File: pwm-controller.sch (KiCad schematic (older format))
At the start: 39 parts, among them J2 OUT-, J4 POWER, J5 OUT+, J6 DEBUG, J7 I2C, SW1 EC12D1524403, U1 78L05, U3 STM8S003F3Px

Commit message: ready to order?
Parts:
- removed J6: DEBUG, Connector_PinHeader_2.54mm:PinHeader_1x05_P2.54mm_Vertical, symbol Connector_Generic:Conn_01x05
- removed J7: I2C, Connector_PinHeader_2.54mm:PinHeader_2x05_P2.54mm_Vertical, symbol Connector_Generic:Conn_02x05_Odd_Even
- removed R10, R11, R13, R14, R19, R21, R22, R6, R7, R8, R9: 4.7k, Resistor_SMD:R_0402_1005Metric, symbol Device:R
- removed TP1: TP5V, TestPoint:TestPoint_Pad_D2.0mm, symbol Connector:TestPoint
- added C3: 3.3n, Capacitor_SMD:C_0402_1005Metric, symbol Device:C
- added D1: B5819W SL, Diode_SMD:D_SOD-123, symbol Device:D_Schottky
- added H3, H6: M2, MountingHole:MountingHole_2mm, symbol Mechanical:MountingHole
- added H8: M2, MountingHole:MountingHole_2.2mm_M2, symbol Mechanical:MountingHole
- added J1: DEBUG_ADDRESS_I2C_INT, Connector_PinHeader_2.54mm:PinHeader_2x09_P2.54mm_Horizontal, symbol Connector_Generic:Conn_02x09_Odd_Even
- added R1, R2: 220, Resistor_SMD:R_0402_1005Metric, symbol Device:R
- renumbered C6 to C1, C8 to C2, C1 to C4, C2 to C5, C7 to C6, C21 to C7, C22 to C8, C23 to C9, D1 to D2, D2 to D3, H5 to H4, H4 to H5, J2 to J6, R4 to R3, R5 to R4, R1 to R5, R3 to R6, R17 to R7, U3 to U1, U1 to U2
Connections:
- net GND: now also C3.1, J1.10 (Pin_10), J1.11 (Pin_11), J1.12 (Pin_12), J1.4 (Pin_4), J1.6 (Pin_6), J1.8 (Pin_8)
- net INT: now also C3.2, J1.13 (Pin_13), J1.14 (Pin_14)
- net PWM1: now also U1.10 (PA3/PWM1); no longer U1.20 (PD3/PWM2)
- net PWM2: now also U1.20 (PD3/PWM2); no longer U1.10 (PA3/PWM1)
- net RE_B: now also U1.13 (PC3/RE_B); no longer U1.19 (PD2/SADD0)
- net RE_I: now also U1.15 (PC5/RE_I); no longer U1.16 (PC6/SADD2)
- net RE_Q: now also U1.14 (PC4/RE_Q); no longer U1.17 (PC7/SADD1)
- net SADD0: now also U1.19 (PD2/SADD0), J1.5 (Pin_5); no longer U1.15 (PC5/RE_I)
- net SADD1: now also U1.17 (PC7/SADD1), J1.7 (Pin_7); no longer U1.14 (PC4/RE_Q)
- net SADD2: now also U1.16 (PC6/SADD2), J1.9 (Pin_9); no longer U1.13 (PC3/RE_B)
- net SCL: now also J1.15 (Pin_15), J1.16 (Pin_16), R1.1; no longer U1.12 (PB4/SCL)
- net SDA: now also J1.17 (Pin_17), J1.18 (Pin_18), R2.1; no longer U1.11 (PB5/SDA)
- net SWIM: now also J1.2 (Pin_2)
- net URX: now also J1.1 (Pin_1)
- net UTX: now also J1.3 (Pin_3)
- net VIN: now also D1.2 (A); no longer C4.1, U2.3 (IN)
- new net SCL_PIN: R1.2, U1.12 (PB4/SCL)
- new net SDA_PIN: R2.2, U1.11 (PB5/SDA)
- new net VIN_D: C4.1, D1.1 (K), U2.3 (IN)
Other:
- note added: "I2C"
- note added: "INT is I2C interrupt for\nslaves to callback on.\ne.g. on user input / boot."
- note added: "IO connector"
- note added: "MCU:\n - Table 21: 5mA @ 16MHz / 1mA @ 2MHz / <1mA @ 128kHz\n - Peripherals approx 1mA extra.\nGPIO: 1mA max loading, per 4.7kΩ pullup\n\nInternal pullups 30-80kΩ (§9.3.6)."
- note removed: "Debug"
- note removed: "I2C and master/slave/address config"
- note removed: "INT is I2C interrupt for\nslaves to callback on."
- note removed: "MCU:\n - Table 21: 5mA @ 16MHz / 1mA @ 2MHz / <1mA @ 128kHz\n - Peripherals approx 1mA extra.\nGPIO: 1mA max loading, per 4.7kΩ pullup\n\nInternal pullups 30-80kΩ (§9.3.6), could use those\nfor all except I2C, instead of 4.7kΩ resistors. Would\nconsiderably improve the routing."
- note removed: "Slave interrupt"
- moved on the sheet: C1, C2, C4, C5, C6, C7, C8, C9, H1, H2, H4, H5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

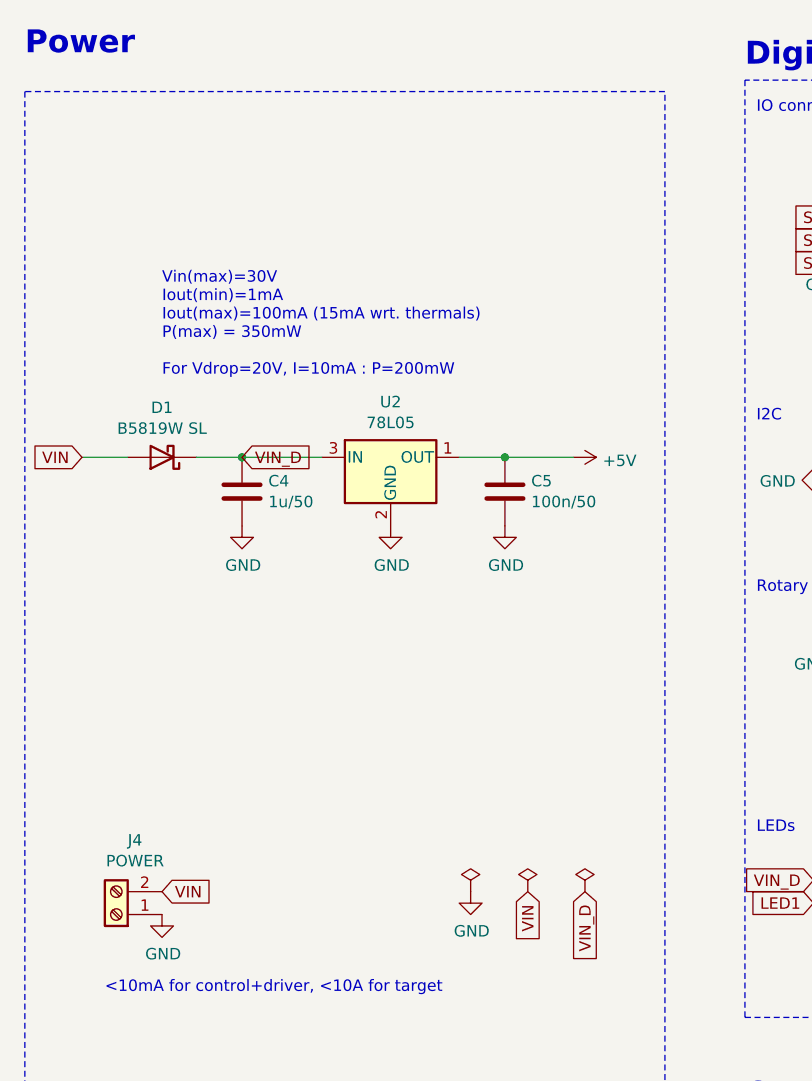
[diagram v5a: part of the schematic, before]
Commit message: moved screw terminals to edge of board, reduced stitching/thermal-via frequency
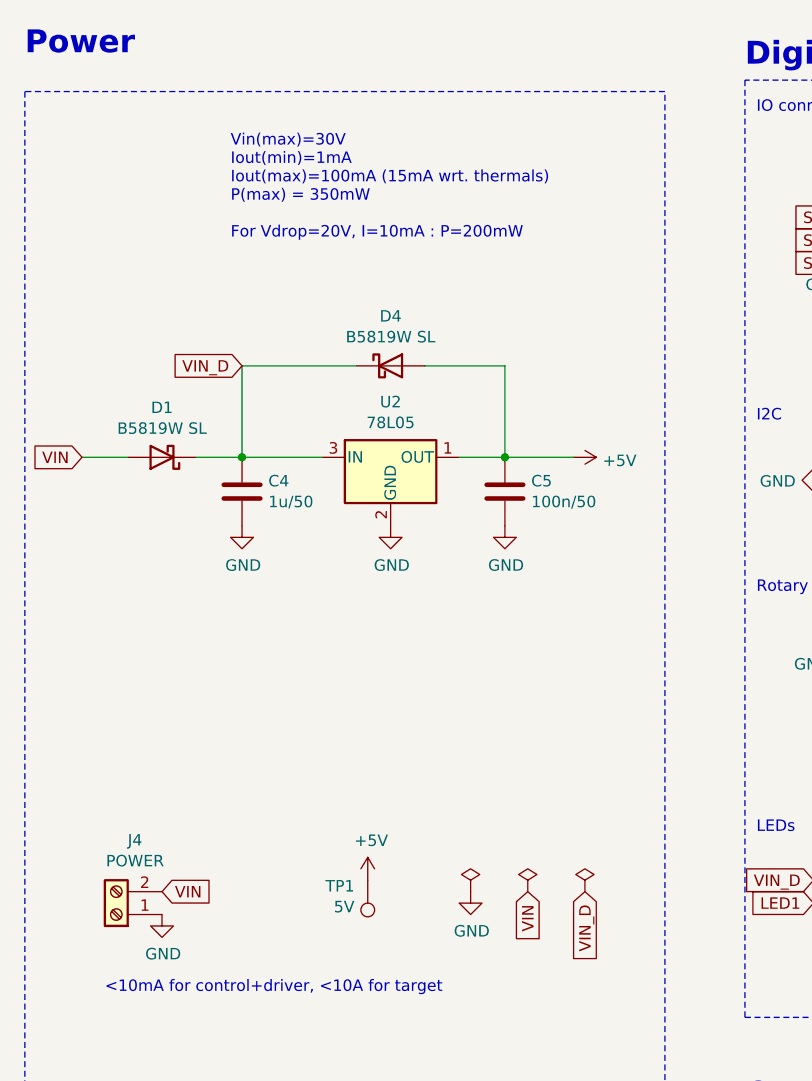
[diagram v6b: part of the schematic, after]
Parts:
- added D4: B5819W SL, Diode_SMD:D_SOD-123, symbol Device:D_Schottky
- added TP1: 5V, TestPoint:TestPoint_THTPad_D1.5mm_Drill0.7mm, symbol Connector:TestPoint
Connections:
- net +5V: now also D4.2 (A), TP1.1
- net VIN_D: now also D4.1 (K)
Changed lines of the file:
@@
 	1    0    0    -1
 $EndComp
-Wire Wire Line
-	2700 3450 2900 3450
 Connection ~ 2900 3450
 $Comp
@@
 Text GLabel 1050 3450 0    50   Input ~ 0
 VIN
-Text Notes 1400 3100 0    50   ~ 0
+Text Notes 1700 2500 0    50   ~ 0
 Vin(max)=30V\nIout(min)=1mA\nIout(max)=100mA (15mA wrt. thermals)\nP(max) = 350mW\n\nFor Vdrop=20V, I=10mA : P=200mW
 $Comp
@@
 Wire Wire Line
 	1250 3450 1050 3450
-Text GLabel 1750 3450 2    50   Input ~ 0
+Text GLabel 1750 3050 0    50   Input ~ 0
 VIN_D
 $Comp
@@
 Text GLabel 5950 3650 2    50   Input ~ 0
 SDA
+$Comp
+L Device:D_Schottky D4
+U 1 1 622155D1
+P 2400 3050
+F 0 "D4" H 2400 3267 50  0000 C CNN
+F 1 "B5819W SL" H 2400 3176 50  0000 C CNN
+F 2 "Diode_SMD:D_SOD-123" H 2400 3050 50  0001 C CNN
+F 3 "https://datasheet.lcsc.com/lcsc/1809140216_Changjiang-Electronics-Tech--CJ-B5819W-SL_C8598.pdf" H 2400 3050 50  0001 C CNN
+F 4 "C8598" H 2400 3050 50  0001 C CNN "JLC"
+	1    2400 3050
+	1    0    0    -1
+$EndComp
+Wire Wire Line
+	2250 3050 1750 3050
+Wire Wire Line
+	1750 3050 1750 3450
+Wire Wire Line
+	2700 3450 2900 3450
+Wire Wire Line
+	2550 3050 2900 3050
+Wire Wire Line
+	2900 3050 2900 3450
+$Comp
+L power:+5V #PWR010
+U 1 1 6222B7D6
+P 2300 5300
+F 0 "#PWR010" H 2300 5150 50  0001 C CNN
+F 1 "+5V" H 2315 5473 50  0000 C CNN
+F 2 "" H 2300 5300 50  0001 C CNN
+F 3 "" H 2300 5300 50  0001 C CNN
+	1    2300 5300
+	1    0    0    -1
+$EndComp
+$Comp
+L Connector:TestPoint TP1
+U 1 1 6222D05A
+P 2300 5300
+F 0 "TP1" H 2358 5326 50  0000 L CNN
+F 1 "5V" H 2358 5417 50  0000 L CNN
+F 2 "TestPoint:TestPoint_THTPad_D1.5mm_Drill0.7mm" H 2500 5300 50  0001 C CNN
+F 3 "~" H 2500 5300 50  0001 C CNN
+	1    2300 5300
+	-1   0    0    1
+$EndComp
 $EndSCHEMATC

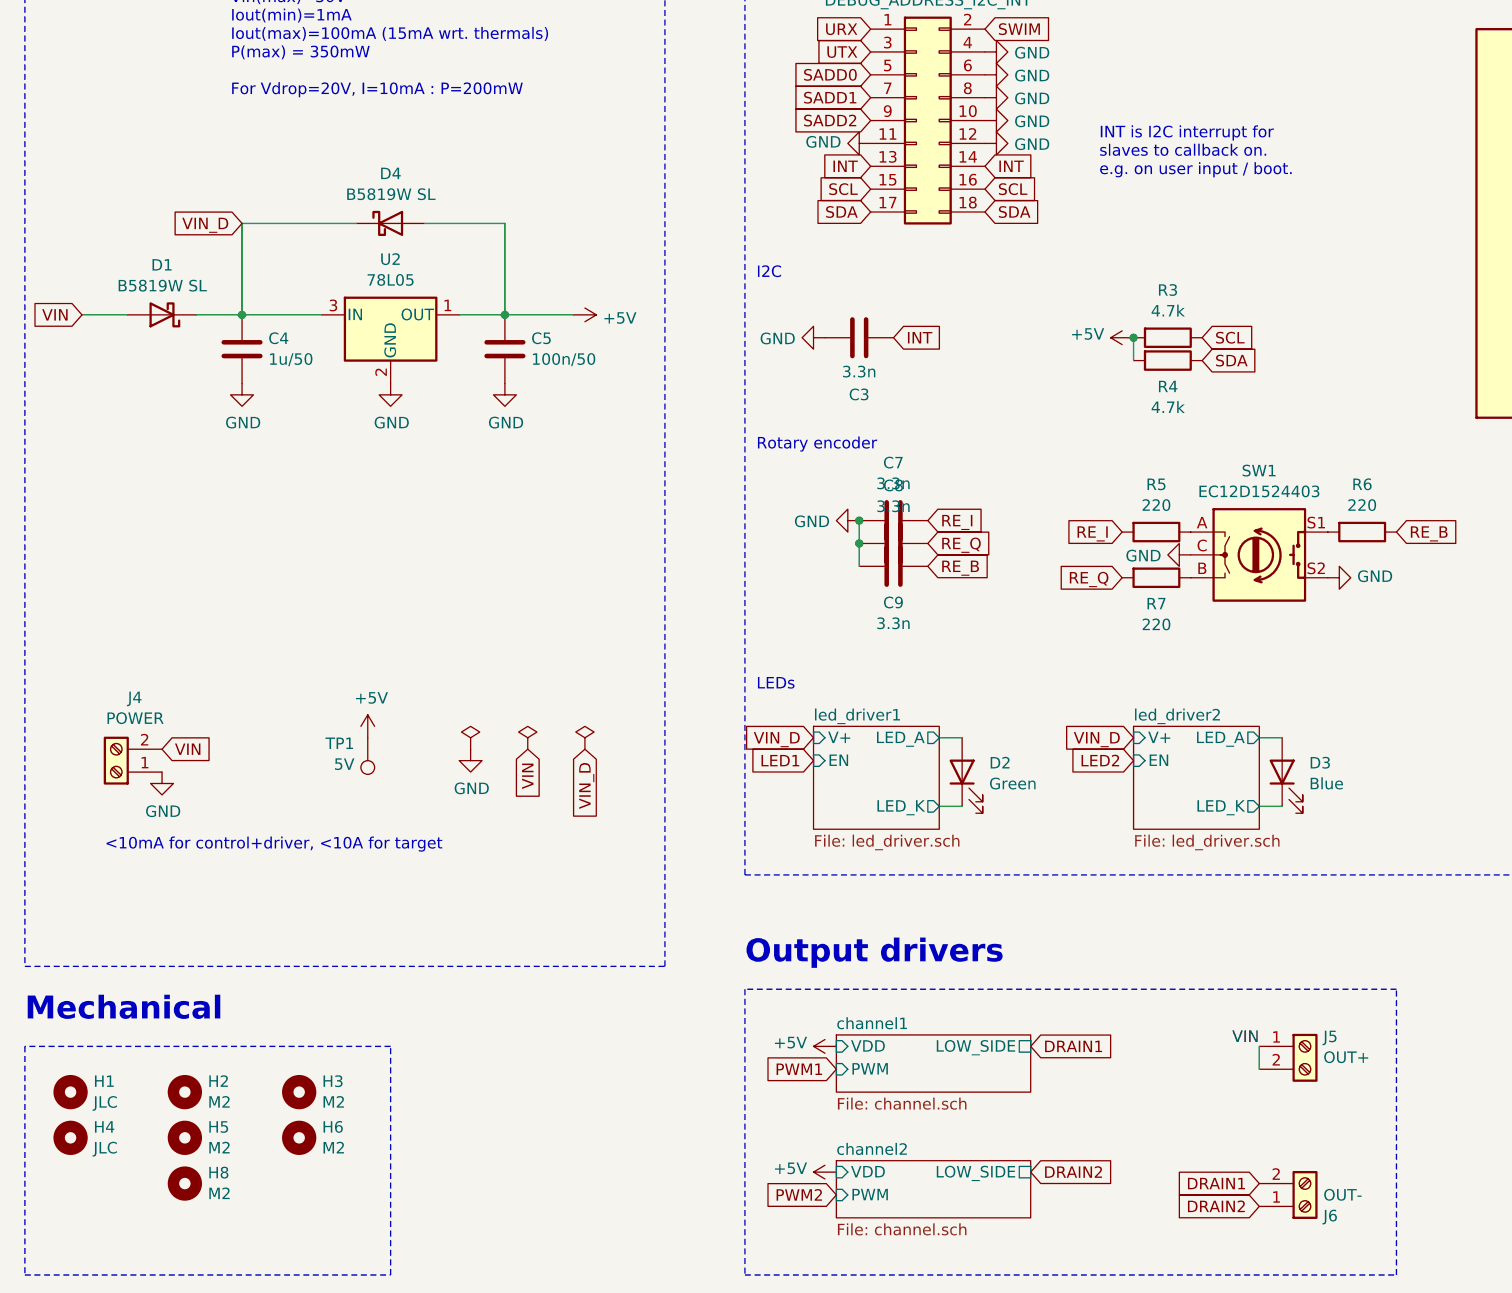
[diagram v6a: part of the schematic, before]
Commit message: we can tolerate higher frequencies as long as our led strips are only a dozen or so metres long
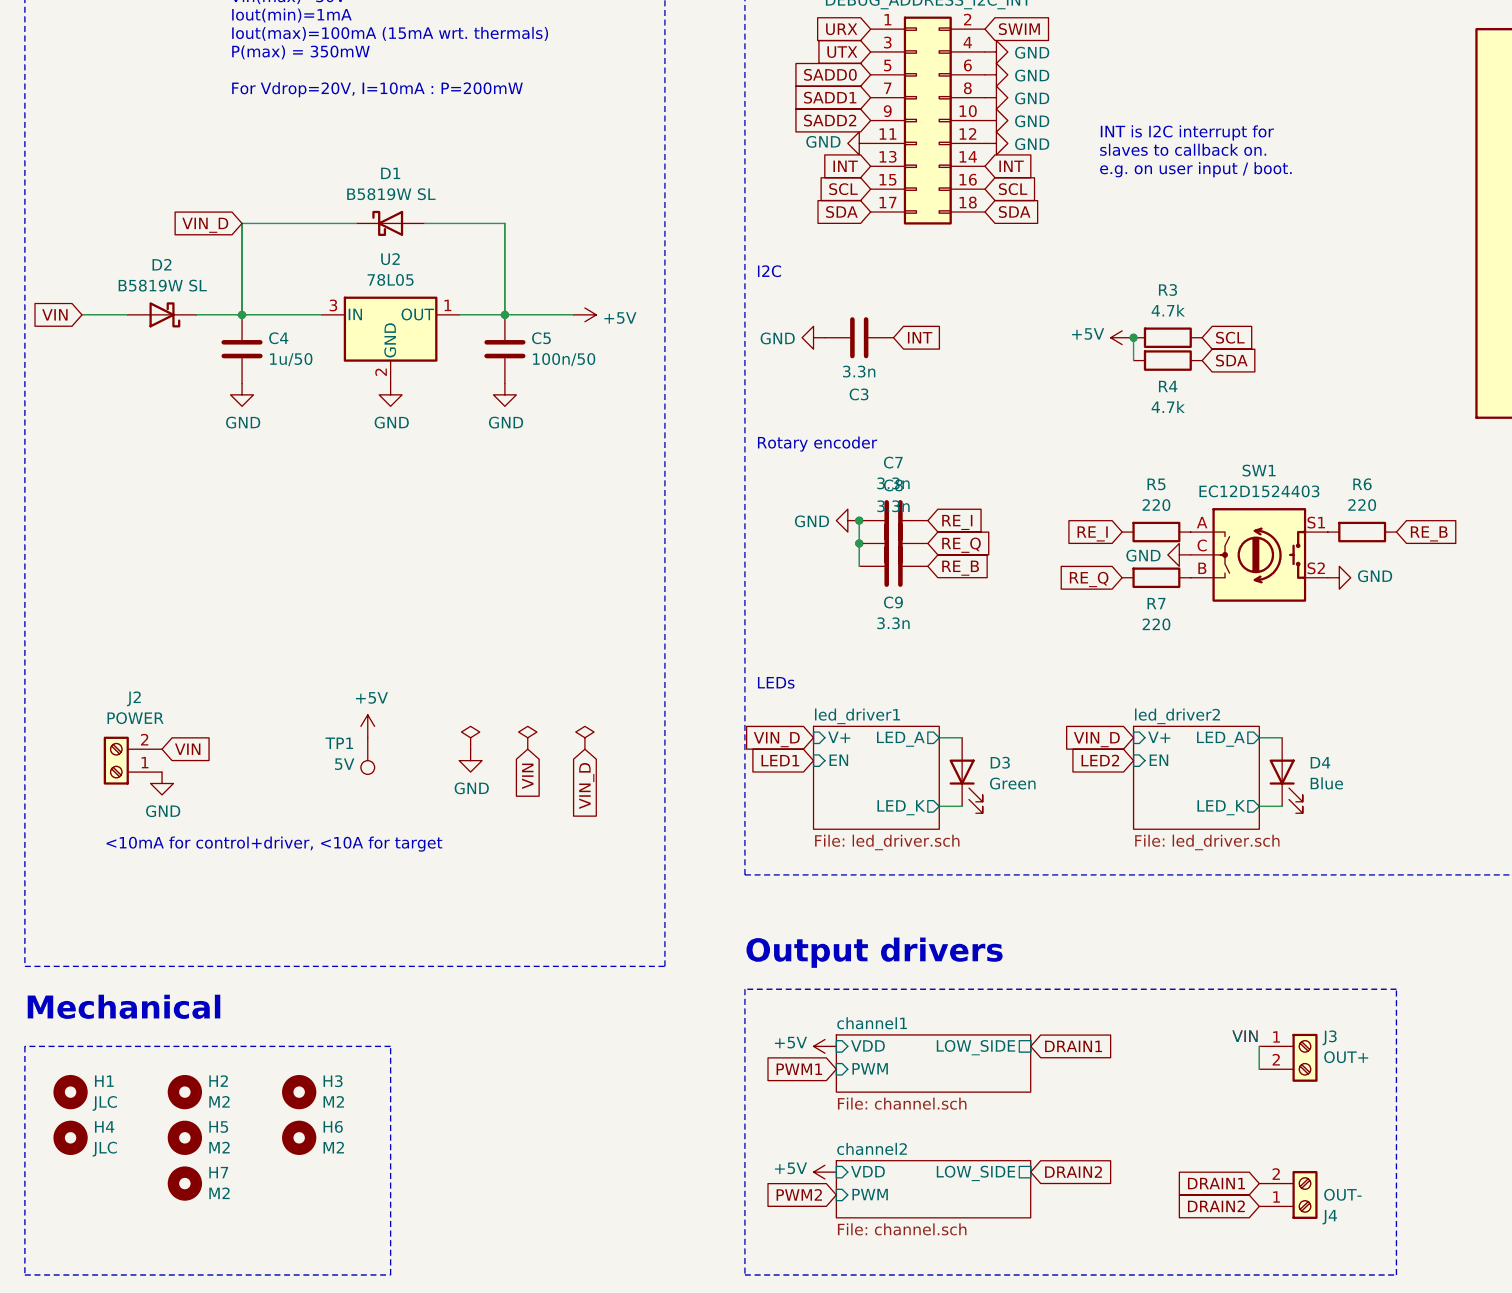
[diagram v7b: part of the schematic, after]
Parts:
- renumbered D4 to D1, D1 to D2, D2 to D3, D3 to D4, H8 to H7, J4 to J2, J5 to J3, J6 to J4
